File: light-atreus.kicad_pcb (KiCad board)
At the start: 2 copper layers, 40.1 x 44.5 mm, 10 parts, among them J1 USB_B, J11 USB_B, J2 CONN_01X02, J3 CONN_01X02, J4 CONN_01X02, J5 CONN_01X02, J6 CONN_01X02, J7 CONN_01X02, J8 CONN_01X02, J9 CONN_01X02

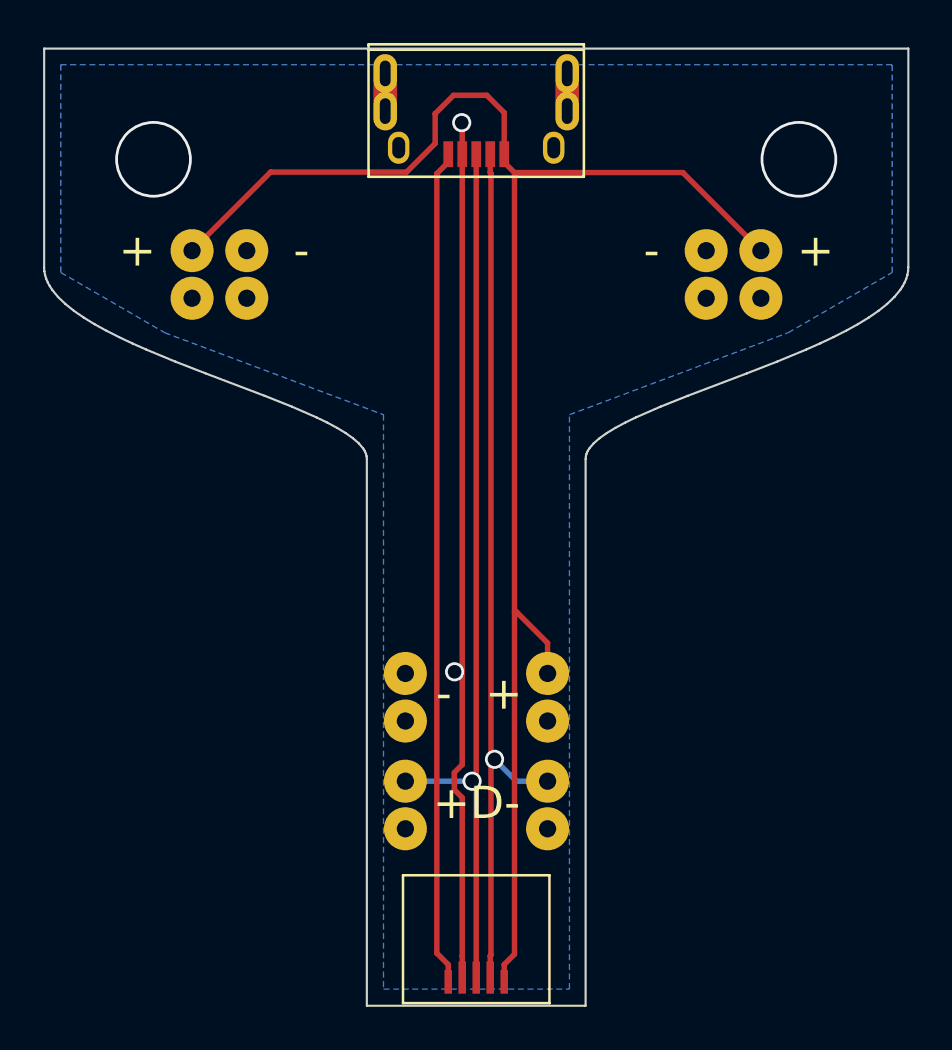
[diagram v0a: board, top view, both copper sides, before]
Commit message: Shorten board by 7mm to account for USB plug housing
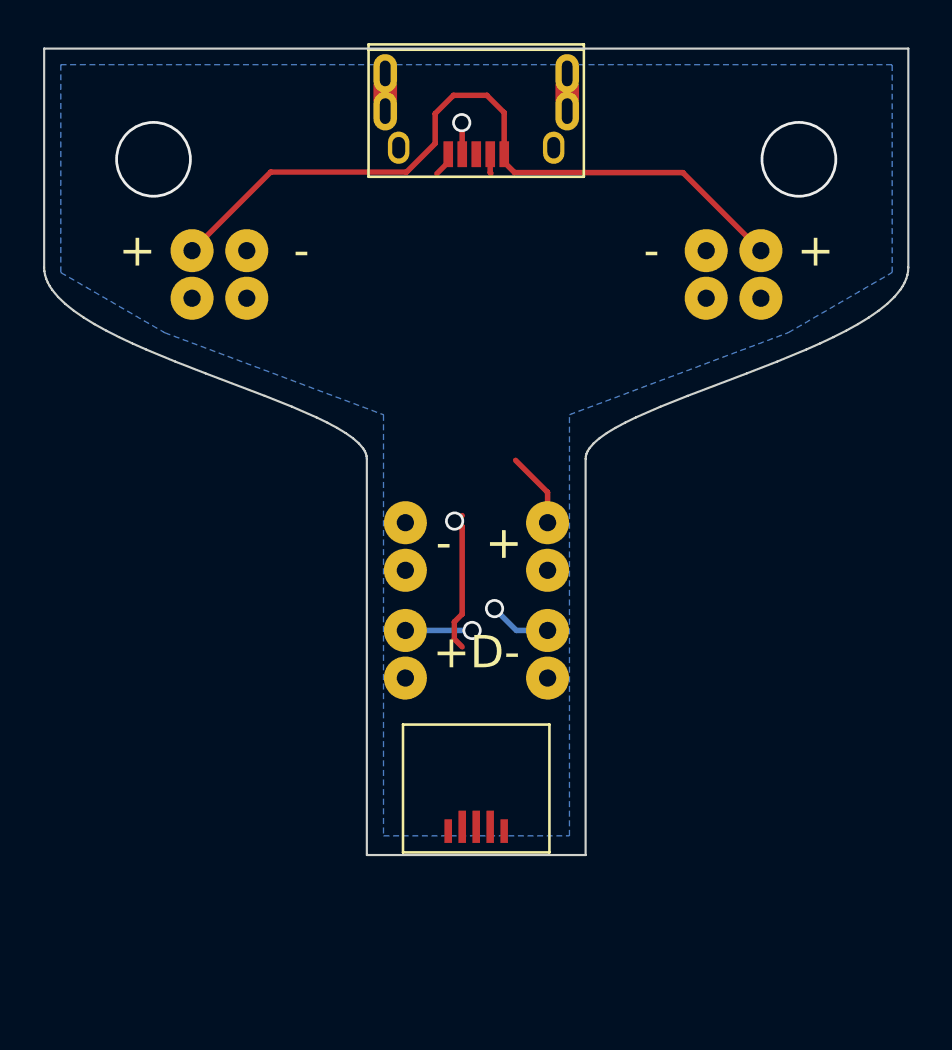
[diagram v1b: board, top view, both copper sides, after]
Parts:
- moved J11 7.00 mm to (130.3, 107.0)
- moved J6 7.00 mm to (133.6, 94.0)
- moved J7 7.00 mm to (127.0, 99.0)
- moved J8 7.00 mm to (133.6, 99.0)
- moved J9 7.00 mm to (127.0, 94.0)
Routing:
- net /D+: track 41.5 -> 3.28 mm
- net /VBUS: track 75.9 -> 38.1 mm
- net /SHIELD: track 38.9 -> 1.12 mm
- net /D-: track 41.2 -> 3.79 mm
- net /GND: track 40.9 -> 8.28 mm
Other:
- board size 40.1 x 44.5 mm -> 40.1 x 37.5 mm
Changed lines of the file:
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@@
     (thickness 1.6)
     (drawings 73)
-    (tracks 53)
+    (tracks 38)
     (zones 0)
     (modules 10)
@@
   )
   (module custom_footprints:SolderWirePad_1x2-8mm (layer F.Cu)
-    (at 133.604 101.008 270)
+    (at 133.604 94.008 270)
     (fp_text reference J6 (at 0 -3.81 270) (layer Cmts.User)
       (effects (font (size 1 1) (thickness 0.15)))
@@
   )
   (module custom_footprints:SolderWirePad_1x2-8mm (layer F.Cu)
-    (at 127 106.012 270)
+    (at 127 99.012 270)
     (fp_text reference J7 (at 0 -3.81 270) (layer Cmts.User)
       (effects (font (size 1 1) (thickness 0.15)))
@@
   )
   (module custom_footprints:SolderWirePad_1x2-8mm (layer F.Cu)
-    (at 133.604 106.012 270)
+    (at 133.604 99.012 270)
     (fp_text reference J8 (at 0 -3.81 270) (layer Cmts.User)
       (effects (font (size 1 1) (thickness 0.15)))
@@
   )
   (module custom_footprints:SolderWirePad_1x2-8mm (layer F.Cu)
-    (at 127 101.008 270)
+    (at 127 94.008 270)
     (fp_text reference J9 (at 0 -3.81 270) (layer Cmts.User)
       (effects (font (size 1 1) (thickness 0.15)))
@@
   )
   (module custom_footprints:USB_Micro-B-custom-plug locked (layer F.Cu)
-    (at 130.2893 114.0206 180)
+    (at 130.2893 107.0206 180)
     (descr "Micro USB Type B Receptacle")
     (tags "USB USB_B USB_micro USB_OTG")
@@
       (net 5 /VBUS))
   )
-  (gr_text - (at 128.778 100.838) (layer F.SilkS)
-    (effects (font (size 1.5 1.5) (thickness 0.3)))
-  )
-  (gr_text + (at 131.572 100.838) (layer F.SilkS)
-    (effects (font (size 1.5 1.5) (thickness 0.3)))
-  )
-  (gr_text +D- (at 130.302 105.918) (layer F.SilkS)
+  (gr_text - (at 128.778 93.838) (layer F.SilkS)
+    (effects (font (size 1.5 1.5) (thickness 0.3)))
+  )
+  (gr_text + (at 131.572 93.838) (layer F.SilkS)
+    (effects (font (size 1.5 1.5) (thickness 0.3)))
+  )
+  (gr_text +D- (at 130.302 98.918) (layer F.SilkS)
     (effects (font (size 1.5 1.5) (thickness 0.3)))
   )
@@
   (gr_line (start 150.313625 81.393954) (end 150.260917 81.567989) (layer Edge.Cuts) (width 0.1))
   (gr_line (start 150.345753 81.218117) (end 150.313625 81.393954) (layer Edge.Cuts) (width 0.1))
-  (gr_line (start 125.210615 115.330448) (end 135.370615 115.330448) (layer Edge.Cuts) (width 0.1))
-  (gr_line (start 125.210615 89.930448) (end 125.210615 115.330448) (layer Edge.Cuts) (width 0.1))
+  (gr_line (start 125.210615 108.331) (end 135.370615 108.331) (layer Edge.Cuts) (width 0.1))
+  (gr_line (start 125.210615 89.930448) (end 125.210615 108.331) (layer Edge.Cuts) (width 0.1))
   (gr_line (start 150.188315 81.740251) (end 150.096505 81.910768) (layer Edge.Cuts) (width 0.1))
   (gr_line (start 150.260917 81.567989) (end 150.188315 81.740251) (layer Edge.Cuts) (width 0.1))
@@
   (gr_line (start 113.700372 84.27901) (end 114.319605 84.570892) (layer Edge.Cuts) (width 0.1))
   (gr_line (start 110.224615 81.040448) (end 110.235477 81.218117) (layer Edge.Cuts) (width 0.1))
-  (gr_line (start 135.370615 115.330448) (end 135.370615 89.930448) (layer Edge.Cuts) (width 0.1))
+  (gr_line (start 135.370615 108.331) (end 135.370615 89.930448) (layer Edge.Cuts) (width 0.1))
   (gr_line (start 112.062193 83.37174) (end 112.566177 83.679667) (layer Edge.Cuts) (width 0.1))
   (gr_line (start 111.6076 83.058) (end 112.062193 83.37174) (layer Edge.Cuts) (width 0.1))
@@
   (segment (start 128.9893 76.159) (end 128.9893 75.784) (width 0.254) (layer F.Cu) (net 1))
   (segment (start 128.460498 76.687802) (end 128.9893 76.159) (width 0.254) (layer F.Cu) (net 1))
-  (segment (start 128.9893 113.4166) (end 128.460498 112.887798) (width 0.254) (layer F.Cu) (net 1))
-  (segment (start 128.460498 112.887798) (end 128.460498 76.687802) (width 0.254) (layer F.Cu) (net 1))
-  (segment (start 128.9893 114.2206) (end 128.9893 113.4166) (width 0.254) (layer F.Cu) (net 1))
-  (segment (start 129.286 99.822) (end 129.3853 99.822) (width 0.254) (layer F.Cu) (net 2))
-  (segment (start 129.3853 99.822) (end 129.6393 99.568) (width 0.254) (layer F.Cu) (net 2))
-  (segment (start 129.6393 100.076) (end 129.6393 104.139758) (width 0.254) (layer F.Cu) (net 2))
-  (segment (start 129.6393 100.076) (end 129.54 100.076) (width 0.254) (layer F.Cu) (net 2))
-  (segment (start 129.6393 75.784) (end 129.6393 100.076) (width 0.254) (layer F.Cu) (net 2))
-  (segment (start 129.54 100.076) (end 129.286 99.822) (width 0.254) (layer F.Cu) (net 2))
-  (via (at 129.286 99.822) (size 0.889) (drill 0.635) (layers F.Cu B.Cu) (net 2))
-  (segment (start 129.6393 105.664242) (end 129.6393 113.0166) (width 0.254) (layer F.Cu) (net 2))
-  (segment (start 129.273299 105.298241) (end 129.6393 105.664242) (width 0.254) (layer F.Cu) (net 2))
-  (segment (start 129.273299 104.505759) (end 129.273299 105.298241) (width 0.254) (layer F.Cu) (net 2))
-  (segment (start 129.6393 104.139758) (end 129.273299 104.505759) (width 0.254) (layer F.Cu) (net 2))
-  (segment (start 129.6393 113.0166) (end 129.6393 114.0206) (width 0.254) (layer F.Cu) (net 2))
+  (segment (start 129.286 92.822) (end 129.3853 92.822) (width 0.254) (layer F.Cu) (net 2))
+  (segment (start 129.3853 92.822) (end 129.6393 92.568) (width 0.254) (layer F.Cu) (net 2))
+  (segment (start 129.6393 93.076) (end 129.6393 97.139758) (width 0.254) (layer F.Cu) (net 2))
+  (segment (start 129.6393 93.076) (end 129.54 93.076) (width 0.254) (layer F.Cu) (net 2))
+  (segment (start 129.54 93.076) (end 129.286 92.822) (width 0.254) (layer F.Cu) (net 2))
+  (via (at 129.286 92.822) (size 0.889) (drill 0.635) (layers F.Cu B.Cu) (net 2))
+  (segment (start 129.273299 98.298241) (end 129.6393 98.664242) (width 0.254) (layer F.Cu) (net 2))
+  (segment (start 129.273299 97.505759) (end 129.273299 98.298241) (width 0.254) (layer F.Cu) (net 2))
+  (segment (start 129.6393 97.139758) (end 129.273299 97.505759) (width 0.254) (layer F.Cu) (net 2))
   (segment (start 129.6393 75.784) (end 129.6393 74.3435) (width 0.254) (layer F.Cu) (net 2))
   (segment (start 129.6393 74.3435) (end 129.6162 74.3204) (width 0.254) (layer F.Cu) (net 2))
   (via (at 129.6162 74.3204) (size 0.889) (drill 0.635) (layers F.Cu B.Cu) (net 2))
-  (segment (start 127 104.902) (end 130.0988 104.902) (width 0.254) (layer B.Cu) (net 3))
-  (segment (start 130.2766 104.902) (end 130.0988 104.902) (width 0.254) (layer B.Cu) (net 3))
-  (via (at 130.0988 104.902) (size 0.889) (drill 0.635) (layers F.Cu B.Cu) (net 3))
-  (segment (start 130.2893 75.784) (end 130.2893 114.0206) (width 0.254) (layer F.Cu) (net 3))
-  (segment (start 133.604 104.902) (end 132.1562 104.902) (width 0.254) (layer B.Cu) (net 4))
-  (segment (start 132.1562 104.902) (end 131.1402 103.886) (width 0.254) (layer B.Cu) (net 4))
-  (via (at 131.1402 103.886) (size 0.889) (drill 0.635) (layers F.Cu B.Cu) (net 4))
-  (segment (start 130.975101 112.980799) (end 130.9393 113.0166) (width 0.254) (layer F.Cu) (net 4))
+  (segment (start 127 97.902) (end 130.0988 97.902) (width 0.254) (layer B.Cu) (net 3))
+  (segment (start 130.2766 97.902) (end 130.0988 97.902) (width 0.254) (layer B.Cu) (net 3))
+  (via (at 130.0988 97.902) (size 0.889) (drill 0.635) (layers F.Cu B.Cu) (net 3))
+  (segment (start 133.604 97.902) (end 132.1562 97.902) (width 0.254) (layer B.Cu) (net 4))
+  (segment (start 132.1562 97.902) (end 131.1402 96.886) (width 0.254) (layer B.Cu) (net 4))
+  (via (at 131.1402 96.886) (size 0.889) (drill 0.635) (layers F.Cu B.Cu) (net 4))
   (segment (start 130.9393 76.638) (end 130.975101 76.673801) (width 0.254) (layer F.Cu) (net 4))
   (segment (start 130.9393 75.784) (end 130.9393 76.638) (width 0.254) (layer F.Cu) (net 4))
-  (segment (start 130.9393 113.0166) (end 130.9393 114.0206) (width 0.254) (layer F.Cu) (net 4))
-  (segment (start 130.975101 76.673801) (end 130.975101 112.980799) (width 0.254) (layer F.Cu) (net 4))
   (segment (start 117.094 80.264) (end 120.74299 76.61501) (width 0.254) (layer F.Cu) (net 5))
   (segment (start 120.74299 76.61501) (end 127.054226 76.61501) (width 0.254) (layer F.Cu) (net 5))
@@
   (segment (start 143.51 80.264) (end 139.884 76.638) (width 0.254) (layer F.Cu) (net 5))
   (segment (start 139.884 76.638) (end 132.0683 76.638) (width 0.254) (layer F.Cu) (net 5))
-  (segment (start 132.0683 76.638) (end 132.0683 97.0026) (width 0.254) (layer F.Cu) (net 5))
-  (segment (start 132.0683 97.0026) (end 132.0683 112.9376) (width 0.254) (layer F.Cu) (net 5))
-  (segment (start 133.604 99.898) (end 133.604 98.484508) (width 0.254) (layer F.Cu) (net 5))
-  (segment (start 133.604 98.484508) (end 132.122092 97.0026) (width 0.254) (layer F.Cu) (net 5))
-  (segment (start 132.122092 97.0026) (end 132.0683 97.0026) (width 0.254) (layer F.Cu) (net 5))
-  (segment (start 131.5893 113.4166) (end 131.5893 114.2206) (width 0.254) (layer F.Cu) (net 5))
-  (segment (start 132.0683 112.9376) (end 131.5893 113.4166) (width 0.254) (layer F.Cu) (net 5))
+  (segment (start 133.604 92.898) (end 133.604 91.484508) (width 0.254) (layer F.Cu) (net 5))
+  (segment (start 133.604 91.484508) (end 132.122092 90.0026) (width 0.254) (layer F.Cu) (net 5))
   (segment (start 131.5893 76.159) (end 132.0683 76.638) (width 0.254) (layer F.Cu) (net 5))
   (segment (start 131.5893 75.784) (end 131.5893 76.159) (width 0.254) (layer F.Cu) (net 5))
@@
     (polygon
       (pts
-        (xy 115.824 84.074) (xy 125.984 87.884) (xy 125.984 114.554) (xy 134.62 114.554) (xy 134.62 87.884)
+        (xy 115.824 84.074) (xy 125.984 87.884) (xy 125.984 107.442) (xy 134.62 107.442) (xy 134.62 87.884)
         (xy 144.78 84.074) (xy 149.606 81.28) (xy 149.606 71.628) (xy 110.998 71.628) (xy 110.998 81.28)
       )
